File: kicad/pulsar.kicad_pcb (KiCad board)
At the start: 2 copper layers, 57 parts, among them J2 NRF-SWD, J3 XO2-JTAG, J4 CONN-2x5, Q1 NMOS, Q10 NMOS, Q11 NMOS, Q12 NMOS, Q2 NMOS, Q3 NMOS, Q4 NMOS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

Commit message: more layouting
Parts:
- added AE1: ANT, libs:ANT3216, F.Cu at (108.0, 95.5)
- added B1: nRF-BALUN, libs:BALUN-2450BM14E0003, F.Cu at (100.1, 96.1)
- added C26: 1u, SMD-1005:SMD-1005, F.Cu at (85.0, 97.0)
- added J1: POWER, libs:TERM-2-3.5-PTH, F.Cu at (125.0, 60.0)
- added J5: CONN-4, libs:CONN-4-2.54-0.8-PTH, F.Cu at (165.0, 120.0)
- added J6: CONN-4, libs:CONN-4-2.54-0.8-PTH, F.Cu at (190.0, 97.5)
- added J7: CONN-4, libs:CONN-4-2.54-0.8-PTH, F.Cu at (190.0, 82.5)
- added J8: CONN-4, libs:CONN-4-2.54-0.8-PTH, F.Cu at (170.0, 67.5)
- added S1: TACTILE-4, libs:TACT-4632, F.Cu at (80.0, 112.5)
- added S2: TACTILE-4, libs:TACT-4632, F.Cu at (72.5, 112.5)
- added Y1: 32kHz, libs:OSC2012, F.Cu at (93.0, 89.2)
- C1: value 1u -> 10u
- C12, C13, C14, C2, C3, C4, C7, C8: value C -> 100n
- C15, C5: value C -> 1u
- C16, C17: value 12pF -> 7p
- C18, C21, C24: value 100nF -> 100n
- C19, C20: value 12pF -> 6p
- C22: value 47nF -> 47n
- C23: value 2.2nF -> 2.2n
- C25: value 1nF -> 1n
- C6: value 2.2u -> 4.7u
- J2, J3: moved to B.Cu
- Y2: value 16MHz -> 32MHz; footprint osc2520:OSC2520 -> libs:OSC2016
- moved R1 63.5 mm to (130.0, 69.8)
- moved R2 63.5 mm to (131.5, 69.8)
- moved R3 63.5 mm to (125.8, 67.5)
- moved U1 63.5 mm to (125.8, 71.5)
- moved C5 47.8 mm to (162.2, 85.0), turned to 180 degrees
- moved C1 47.8 mm to (104.5, 66.2)
- moved C6 47.8 mm to (111.8, 66.5)
- moved FB1 47.8 mm to (103.0, 66.2)
- moved U3 47.8 mm to (108.0, 66.5)
- moved RT1 38.6 mm to (144.5, 108.0)
- moved C15 36.2 mm to (162.8, 95.0)
- moved Q1 29.4 mm to (161.5, 115.2), turned to 180 degrees
- moved Q2 27.8 mm to (165.0, 115.2), turned to 180 degrees
- moved Q3 27.1 mm to (168.5, 115.2), turned to 180 degrees
- moved Q4 26.9 mm to (185.2, 101.0), turned to 270 degrees
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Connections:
- C16 pad 1: PGND -> Net-(C16-Pad1)
- C16 pad 2: Net-(C16-Pad2) -> PGND
- C17 pad 1: PGND -> Net-(C17-Pad1)
- C17 pad 2: Net-(C17-Pad2) -> PGND
- C19 pad 1: PGND -> Net-(C19-Pad1)
- C19 pad 2: Net-(C19-Pad2) -> PGND
- C20 pad 1: PGND -> Net-(C20-Pad1)
- C20 pad 2: Net-(C20-Pad2) -> PGND
- U4 pad 11: Net-(U4-Pad11) -> /BUTTON1
- U4 pad 14: Net-(U4-Pad14) -> /BUTTON2
- U4 pad 15: Net-(U4-Pad15) -> /LED1
- U4 pad 16: /BUTTON1 -> /LED2
- U4 pad 17: /BUTTON2 -> /LED3
- U4 pad 19: /LED1 -> Net-(U4-Pad19)
- U4 pad 20: /LED2 -> /~XO2_RESET
- U4 pad 21: /LED3 -> /~XO2_JTAG_EN
- U4 pad 37: Net-(C19-Pad2) -> Net-(C19-Pad1)
- U4 pad 38: Net-(C20-Pad2) -> Net-(C20-Pad1)
- U4 pad 45: Net-(C16-Pad2) -> Net-(C16-Pad1)
- U4 pad 46: Net-(C17-Pad2) -> Net-(C17-Pad1)
- Y2 pad 1: Net-(C19-Pad2) -> Net-(C19-Pad1)
- Y2 pad 2: PGND -> Net-(Y2-Pad2)
- Y2 pad 3: Net-(C20-Pad2) -> Net-(C20-Pad1)
- Y2 pad 4: PGND -> Net-(Y2-Pad4)

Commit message: more layout
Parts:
- added TERM-2: VAL**, libs:TERM-2-3.5-PTH, F.Cu at (180.8, 85.5)
- added TERM-2: VAL**, libs:TERM-2-3.5-PTH, F.Cu at (180.8, 76.5)
- added TERM-2: VAL**, libs:TERM-2-3.5-PTH, F.Cu at (180.8, 94.5)
- added TERM-2: VAL**, libs:TERM-2-3.5-PTH, F.Cu at (180.8, 103.5)
- moved S2 58.1 mm to (123.0, 83.8), turned to 180 degrees
- moved S1 39.5 mm to (94.5, 75.8), turned to 270 degrees
- moved J4 38.0 mm to (106.0, 115.2), turned to 180 degrees
- moved J3 31.6 mm to (149.0, 46.5)
- moved D1 25.7 mm to (106.0, 88.2), turned to 180 degrees
- moved C26 25.6 mm to (110.5, 99.2), turned to 90 degrees
- moved D2 23.9 mm to (104.5, 88.2), turned to 180 degrees
- moved C20 22.4 mm to (94.5, 108.8), turned to 270 degrees
- moved D3 22.4 mm to (103.0, 88.2), turned to 180 degrees
- moved C17 22.3 mm to (104.5, 107.0), turned to 0 degrees
- moved R5 22.1 mm to (106.0, 90.8), turned to 180 degrees
- moved J7 21.6 mm to (170.0, 74.2), turned to 180 degrees
- moved AE1 21.2 mm to (87.5, 100.8), turned to 180 degrees
- moved RT1 20.6 mm to (155.0, 90.2)
- moved Y1 20.1 mm to (102.5, 107.0), turned to 0 degrees
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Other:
- board outline added: 50 x 50 mm

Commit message: antenna feed calculations
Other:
- board text added: "50R Antenna feed on FR-4 1.2mm/1.6mm: coplanar wave guide with ground plane, 750um conductor, 160um spacing (see antenna_waveguide.xsctn)"
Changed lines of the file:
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@@
     (area 0 0 0 0)
     (thickness 1.6)
-    (drawings 7)
+    (drawings 8)
     (tracks 0)
     (zones 0)
@@
     (pad 2 thru_hole oval (at 1.75 0 90) (size 2 2.6) (drill 1.2) (layers *.Cu *.Mask))
   )
+  (gr_text "50R Antenna feed on FR-4 1.2mm/1.6mm:\ncoplanar wave guide with ground plane,\n750um conductor, 160um spacing\n(see antenna_waveguide.xsctn)" (at 25.75 81.25) (layer Cmts.User)
+    (effects (font (size 1.5 1.5) (thickness 0.05)) (justify left))
+  )
   (gr_circle (center 212.25 124.75) (end 214.75 124.75) (layer Dwgs.User) (width 0.2))

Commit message: layout progress
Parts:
- removed TERM-2 (x4): VAL**, libs:TERM-2-3.5-PTH
- added J13: CONN-2, libs:TERM-2-3.5-PTH, F.Cu at (146.0, 139.2)
- added J14: CONN-2, libs:TERM-2-3.5-PTH, F.Cu at (146.0, 129.8)
- added J15: CONN-2, libs:TERM-2-3.5-PTH, F.Cu at (146.0, 120.2)
- added J16: CONN-2, libs:TERM-2-3.5-PTH, F.Cu at (146.0, 110.8)
- added MH1: MOUNTHOLE, libs:HOLE-M3-COND, F.Cu at (135.0, 135.0)
- added MH2: MOUNTHOLE, libs:HOLE-M3-COND, F.Cu at (115.0, 135.0)
- added MH3: MOUNTHOLE, libs:HOLE-M3-COND, F.Cu at (115.0, 115.0)
- added MH4: MOUNTHOLE, libs:HOLE-M3-COND, F.Cu at (135.0, 115.0)
- C1: footprint SMD-1005:SMD-1005 -> SMD-2012:SMD-2012
- R1, R2: footprint SMD-1608:SMD-1608 -> SMD-1005:SMD-1005
- moved J3 72.0 mm to (122.0, 113.2), turned to 90 degrees
- moved Q1 56.0 mm to (128.0, 143.0)
- moved Q7 53.3 mm to (139.5, 120.0), turned to 270 degrees
- moved Q2 50.5 mm to (131.5, 143.0)
- moved Q3 50.5 mm to (135.0, 143.0)
- moved Q4 50.4 mm to (138.5, 143.0), turned to 180 degrees
- moved C12 50.2 mm to (133.0, 130.0)
- moved C13 50.2 mm to (126.8, 125.5)
- moved C14 50.2 mm to (126.8, 126.5)
- moved C15 50.2 mm to (132.0, 130.0)
- moved C2 50.2 mm to (136.8, 123.2)
- moved C3 50.2 mm to (136.8, 125.8)
- moved C4 50.2 mm to (130.5, 120.0)
- moved C7 50.2 mm to (126.8, 123.8)
- moved C8 50.2 mm to (136.8, 126.8)
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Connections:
- net Net-(J5-Pad2) renamed /rgb1/CH1_OUT
- net Net-(J5-Pad3) renamed /rgb1/CH2_OUT
- net Net-(J5-Pad4) renamed /rgb1/CH3_OUT
- net Net-(J6-Pad2) renamed /rgb2/CH1_OUT
- net Net-(J6-Pad3) renamed /rgb2/CH2_OUT
- net Net-(J6-Pad4) renamed /rgb2/CH3_OUT
- net Net-(J7-Pad2) renamed /rgb3/CH1_OUT
- net Net-(J7-Pad3) renamed /rgb3/CH2_OUT
- net Net-(J7-Pad4) renamed /rgb3/CH3_OUT
- net Net-(J8-Pad2) renamed /rgb4/CH1_OUT
- net Net-(J8-Pad3) renamed /rgb4/CH2_OUT
- net Net-(J8-Pad4) renamed /rgb4/CH3_OUT
- C10 pad 1: /IIN_SENSE -> /VIN_SENSE
- C11 pad 1: /TEMP_SENSE -> /IIN_SENSE
- C9 pad 1: /VIN_SENSE -> /TEMP_SENSE
- J2 pad 10: Net-(J2-Pad10) -> (no net)
- J2 pad 7: Net-(J2-Pad7) -> (no net)
- J2 pad 9: Net-(J2-Pad9) -> (no net)
- J3 pad 7: Net-(J3-Pad7) -> (no net)
- J4 pad 1: /AUX1 -> +3V3
- J4 pad 3: /AUX2 -> /AUX1
- J4 pad 5: /AUX3 -> /AUX2
- J4 pad 7: /AUX4 -> /AUX3
- J4 pad 9: /AUX5 -> /AUX4
- S1 pad 2: Net-(S1-Pad2) -> (no net)
- S2 pad 2: Net-(S2-Pad2) -> (no net)
- U3 pad 4: Net-(U3-Pad4) -> (no net)
- U4 pad 10: Net-(U4-Pad10) -> (no net)
- U4 pad 11: /BUTTON1 -> (no net)
- U4 pad 14: /BUTTON2 -> (no net)
- U4 pad 18: Net-(U4-Pad18) -> /BUTTON1
- U4 pad 19: Net-(U4-Pad19) -> /BUTTON2
- U4 pad 2: Net-(U4-Pad2) -> (no net)
- U4 pad 3: /AUX5 -> /AUX1
- U4 pad 31: Net-(B1-Pad3) -> Net-(B1-Pad4)
- U4 pad 32: Net-(B1-Pad4) -> Net-(B1-Pad3)
- U4 pad 4: /AUX1 -> /AUX2
- U4 pad 5: /AUX2 -> (no net)
- U4 pad 6: /VIN_SENSE -> /TEMP_SENSE
- U4 pad 7: /IIN_SENSE -> /VIN_SENSE
- U4 pad 8: /TEMP_SENSE -> /IIN_SENSE
- U4 pad 9: Net-(U4-Pad9) -> (no net)
- Y2 pad 2: Net-(Y2-Pad2) -> (no net)
- Y2 pad 4: Net-(Y2-Pad4) -> (no net)
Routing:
- net +3V3: track 0.00 -> 24.8 mm
- net /ANT: track 0.00 -> 15.3 mm
- net /VIN_SENSE: track 0.00 -> 14.5 mm
- net /IIN_SENSE: track 0.00 -> 13.1 mm
- net Net-(C17-Pad1): track 0.00 -> 6.34 mm
- net Net-(C20-Pad1): track 0.00 -> 5.91 mm
- net Net-(C16-Pad1): track 0.00 -> 5.90 mm
- net Net-(C19-Pad1): track 0.00 -> 3.51 mm
- net Net-(B1-Pad5): track 0.00 -> 3.40 mm
- net /TEMP_SENSE: track 0.00 -> 3.02 mm
- net Net-(C22-Pad1): track 0.00 -> 2.88 mm
- net Net-(C24-Pad1): track 0.00 -> 2.17 mm
- net Net-(B1-Pad4): track 0.00 -> 1.51 mm
- net Net-(B1-Pad3): track 0.00 -> 1.51 mm
- added copper zone on B.Cu, net DGND
- added copper zone on F.Cu, net DGND
- added copper zone on B.Cu, net VIN
- added copper zone on F.Cu, net VIN
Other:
- net class Default: clearance 0.15 -> 0.1499; trace_width 0.15 -> 0.1499; via_dia 0.6 -> 0.55
- net class antenna feed added: clearance 0.16, trace_width 0.75, via_dia 0.55, via_drill 0.3
- rule trace_clearance: 0.15 -> 0.1499
- rule trace_min: 0.15 -> 0.1499
- rule via_min_size: 0.6 -> 0.55

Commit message: more layout
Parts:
- moved C14 10.9 mm to (137.2, 123.8), turned to 90 degrees
- moved C12 10.3 mm to (130.5, 120.0), turned to 180 degrees
- moved C5 10.0 mm to (135.0, 130.0), turned to 0 degrees
- moved C7 7.72 mm to (133.5, 120.0), turned to 180 degrees
- moved C2 7.29 mm to (134.0, 130.0), turned to 0 degrees
- moved C4 7.29 mm to (137.2, 122.8), turned to 90 degrees
- moved C13 7.27 mm to (131.5, 120.0), turned to 180 degrees
- moved C8 7.27 mm to (130.2, 130.0), turned to 0 degrees
- moved C3 6.95 mm to (131.2, 130.0), turned to 0 degrees
- moved C15 6.05 mm to (127.2, 126.2), turned to 270 degrees
- moved C16 4.17 mm to (117.3, 122.4), turned to 180 degrees
- moved C17 2.24 mm to (113.3, 122.4), turned to 180 degrees
- moved Y1 1.79 mm to (115.3, 122.4), turned to 180 degrees
- moved C19 0.79 mm to (113.2, 129.0)
- moved C20 0.79 mm to (116.8, 129.0)
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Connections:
- B1 pad 2: PGND -> DGND
- B1 pad 6: PGND -> DGND
- C1 pad 2: PGND -> DGND
- C10 pad 2: PGND -> DGND
- C11 pad 2: PGND -> DGND
- C12 pad 2: PGND -> DGND
- C13 pad 2: PGND -> DGND
- C14 pad 2: PGND -> DGND
- C15 pad 2: PGND -> DGND
- C16 pad 2: PGND -> DGND
- C17 pad 2: PGND -> DGND
- C18 pad 2: PGND -> DGND
- C19 pad 2: PGND -> DGND
- C2 pad 2: PGND -> DGND
- C20 pad 2: PGND -> DGND
- C21 pad 2: PGND -> DGND
- C22 pad 2: PGND -> DGND
- C23 pad 2: PGND -> DGND
- C24 pad 2: PGND -> DGND
- C25 pad 2: PGND -> DGND
- C26 pad 2: PGND -> DGND
- C3 pad 2: PGND -> DGND
- C4 pad 2: PGND -> DGND
- C5 pad 2: PGND -> DGND
- C6 pad 2: PGND -> DGND
- C7 pad 2: PGND -> DGND
- C8 pad 2: PGND -> DGND
- C9 pad 2: PGND -> DGND
- D1 pad C: PGND -> DGND
- D2 pad C: PGND -> DGND
- D3 pad C: PGND -> DGND
- J1 pad 2: PGND -> DGND
- J2 pad 3: PGND -> DGND
- J2 pad 5: PGND -> DGND
- J3 pad 2: /XO2_JTAG_TMS -> /rgb2/CH3
- J3 pad 3: PGND -> DGND
- J3 pad 4: /XO2_JTAG_TCK -> /rgb3/CH1
- J3 pad 5: PGND -> DGND
- J3 pad 6: /XO2_JTAG_TDO -> /rgb3/CH3
- J3 pad 8: /XO2_JTAG_TDI -> /rgb3/CH2
- J4 pad 10: PGND -> DGND
- MH1 pad 1: PGND -> DGND
- MH2 pad 1: PGND -> DGND
- MH3 pad 1: PGND -> DGND
- MH4 pad 1: PGND -> DGND
- Q1 pad S: PGND -> DGND
- Q10 pad S: PGND -> DGND
- Q11 pad S: PGND -> DGND
- Q12 pad S: PGND -> DGND
- Q2 pad S: PGND -> DGND
- Q3 pad S: PGND -> DGND
- Q4 pad S: PGND -> DGND
- Q5 pad S: PGND -> DGND
- Q6 pad S: PGND -> DGND
- Q7 pad S: PGND -> DGND
- Q8 pad S: PGND -> DGND
- Q9 pad S: PGND -> DGND
- R2 pad 2: PGND -> DGND
- RT1 pad 2: PGND -> DGND
- S1 pad 3: PGND -> DGND
- S1 pad 4: PGND -> DGND
- S2 pad 3: PGND -> DGND
- S2 pad 4: PGND -> DGND
- U1 pad 1: PGND -> DGND
- U1 pad 2: PGND -> DGND
- U2 pad 1: /XO2_JTAG_TDO -> /rgb3/CH3
- U2 pad 11: /rgb2/CH1 -> (no net)
- U2 pad 12: /rgb2/CH2 -> (no net)
- U2 pad 13: /rgb2/CH3 -> (no net)
- U2 pad 14: /rgb3/CH1 -> /SPI_CS
- U2 pad 16: /SPI_CS -> /SPI_CS_PGM
- U2 pad 20: /rgb3/CH2 -> /rgb1/CH1
- U2 pad 21: /rgb3/CH3 -> /rgb1/CH2
- U2 pad 22: PGND -> DGND
- U2 pad 23: /rgb4/CH1 -> /rgb1/CH3
- U2 pad 27: /rgb4/CH2 -> /rgb2/CH1
- U2 pad 28: /rgb4/CH3 -> /rgb2/CH2
- U2 pad 29: /XO2_JTAG_TMS -> /rgb2/CH3
- U2 pad 3: PGND -> DGND
- U2 pad 30: /XO2_JTAG_TCK -> /rgb3/CH1
- U2 pad 32: /XO2_JTAG_TDI -> /rgb3/CH2
- U2 pad 4: /rgb1/CH1 -> /rgb4/CH1
- U2 pad 5: /rgb1/CH2 -> /rgb4/CH2
- U2 pad 8: /rgb1/CH3 -> /rgb4/CH3
- U2 pad FLAG: PGND -> DGND
- U3 pad 2: PGND -> DGND
- U4 pad 13: PGND -> DGND
- U4 pad 20: /~XO2_RESET -> (no net)
- U4 pad 21: /~XO2_JTAG_EN -> (no net)
- U4 pad 22: /XO2_JTAG_TDO -> (no net)
- U4 pad 27: /XO2_JTAG_TMS -> (no net)
- U4 pad 28: /XO2_JTAG_TCK -> (no net)
- U4 pad 33: PGND -> DGND
- U4 pad 34: PGND -> DGND
- U4 pad 40: /XO2_JTAG_TDI -> /SPI_MOSI
- U4 pad 41: /SPI_CLK -> /SPI_CS_PGM
- U4 pad 42: /SPI_MISO -> /SPI_CS
- U4 pad 43: /SPI_CS -> /SPI_MISO
- U4 pad 44: /SPI_MOSI -> /SPI_CLK
- U4 pad 47: /AUX3 -> /~XO2_RESET
- U4 pad 5: (no net) -> /AUX3
- U4 pad FLAG: PGND -> DGND
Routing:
- net +3V3: track 24.8 -> 57.8 mm
- net /rgb2/CH3_OUT: track 0.00 -> 25.8 mm
- net /rgb3/CH1_OUT: track 0.00 -> 23.2 mm
- net DGND: track 0.00 -> 22.4 mm, vias 0 -> 10
- net /rgb2/CH2_OUT: track 0.00 -> 14.3 mm
- net /rgb2/CH1: track 0.00 -> 13.3 mm, vias 0 -> 2
- net /rgb3/CH2_OUT: track 0.00 -> 12.5 mm
- net /rgb1/CH3: track 0.00 -> 12.1 mm, vias 0 -> 2
- net /rgb3/CH3: track 0.00 -> 11.3 mm, vias 0 -> 2
- net /rgb4/CH1: track 0.00 -> 11.2 mm, vias 0 -> 2
- net /rgb4/CH3: track 0.00 -> 10.7 mm, vias 0 -> 2
- net /rgb4/CH2: track 0.00 -> 10.5 mm, vias 0 -> 2
- net /rgb1/CH2: track 0.00 -> 10.1 mm, vias 0 -> 2
- net /rgb1/CH1: track 0.00 -> 9.62 mm, vias 0 -> 2
- net (no net): track 0.00 -> 8.88 mm, vias 0 -> 1
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- added copper zone on B.Cu, net PGND
- added copper zone on F.Cu, net PGND
- removed copper zone on B.Cu, net DGND
- removed copper zone on F.Cu, net DGND
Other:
- net class high current added: clearance 0.15, trace_width 0.5, via_dia 0.55, via_drill 0.3

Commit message: layout
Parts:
- moved D1 22.8 mm to (102.2, 119.2), turned to 270 degrees
- moved D2 22.3 mm to (102.2, 121.8), turned to 270 degrees
- moved D3 22.1 mm to (102.2, 124.2), turned to 270 degrees
- moved C6 21.5 mm to (101.5, 103.0), turned to 180 degrees
- moved J3 20.2 mm to (138.4, 125.0), turned to 180 degrees
- moved R5 20.1 mm to (104.5, 119.5)
- moved R6 19.4 mm to (104.5, 122.0)
- moved R7 19.0 mm to (104.5, 124.5)
- moved U3 15.6 mm to (104.5, 103.0), turned to 90 degrees
- moved J1 10.8 mm to (115.2, 104.2)
- moved R3 10.5 mm to (122.0, 102.2)
- moved U1 10.5 mm to (122.0, 105.5)
- moved C1 9.42 mm to (107.8, 103.0), turned to 180 degrees
- moved C26 8.00 mm to (113.8, 120.0)
- moved FB1 7.22 mm to (109.5, 102.5), turned to 0 degrees
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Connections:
- C10 pad 1: /VIN_SENSE -> /IIN_SENSE
- C11 pad 1: /IIN_SENSE -> /VIN_SENSE
- J3 pad 2: /rgb2/CH3 -> /XO2_JTAG_TMS
- J3 pad 4: /rgb3/CH1 -> /XO2_JTAG_TCK
- J3 pad 6: /rgb3/CH3 -> /rgb3/CH1
- J3 pad 8: /rgb3/CH2 -> /rgb2/CH3
- S1 pad 1: /BUTTON1 -> (no net)
- S1 pad 2: (no net) -> /BUTTON1
- S2 pad 1: /BUTTON2 -> (no net)
- S2 pad 2: (no net) -> /BUTTON2
- U2 pad 1: /rgb3/CH3 -> /rgb3/CH1
- U2 pad 11: (no net) -> /SPI_CS
- U2 pad 12: (no net) -> /rgb4/CH2
- U2 pad 13: (no net) -> /rgb4/CH3
- U2 pad 14: /SPI_CS -> (no net)
- U2 pad 29: /rgb2/CH3 -> /XO2_JTAG_TMS
- U2 pad 30: /rgb3/CH1 -> /XO2_JTAG_TCK
- U2 pad 32: /rgb3/CH2 -> /rgb2/CH3
- U2 pad 4: /rgb4/CH1 -> /rgb3/CH2
- U2 pad 5: /rgb4/CH2 -> /rgb3/CH3
- U2 pad 8: /rgb4/CH3 -> /rgb4/CH1
- U4 pad 7: /VIN_SENSE -> /IIN_SENSE
- U4 pad 8: /IIN_SENSE -> /VIN_SENSE
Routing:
- net /SPI_CLK: track 3.27 -> 33.3 mm
- net /SPI_MISO: track 3.62 -> 33.0 mm
- net /SPI_CS: track 3.19 -> 31.7 mm
- net /SPI_MOSI: track 2.91 -> 30.4 mm, vias 2 -> 0
- net /IIN_SENSE: track 13.1 -> 40.5 mm, vias 0 -> 2
- net /rgb3/CH1: track 1.00 -> 28.3 mm, vias 1 -> 2
- net VIN: track 0.00 -> 26.5 mm
- net DGND: track 22.4 -> 46.0 mm, vias 10 -> 29
- net /TEMP_SENSE: track 3.02 -> 25.0 mm, vias 0 -> 2
- net /BUTTON1: track 0.00 -> 20.7 mm
- net /RX: track 0.00 -> 20.5 mm, vias 0 -> 1
- net /TX: track 0.30 -> 20.6 mm, vias 0 -> 1
- net /NRF_SWDIO/~RESET: track 0.00 -> 19.8 mm, vias 0 -> 1
- net /rgb2/CH3: track 1.50 -> 21.2 mm, vias 1 -> 2
- net /NRF_SWDCLK: track 0.00 -> 19.7 mm, vias 0 -> 1
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- added copper zone on B.Cu, net DGND
- added copper zone on F.Cu, net DGND
- removed copper zone on B.Cu, net PGND
- removed copper zone on F.Cu, net PGND

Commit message: layout
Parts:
- moved C15 0.25 mm to (123.0, 126.2), turned to 180 degrees
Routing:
- net +3V3: track 51.4 -> 142.8 mm, vias 1 -> 8
- net /~XO2_RESET: track 14.4 -> 57.0 mm, vias 1 -> 3
- net DGND: track 46.0 -> 48.7 mm, vias 29 -> 32
- net /TEMP_SENSE: track 25.0 -> 26.6 mm
- net /rgb1/CH3: track 17.3 -> 18.2 mm
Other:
- net class power supply added: clearance 0.1499, trace_width 0.3, via_dia 0.55, via_drill 0.3

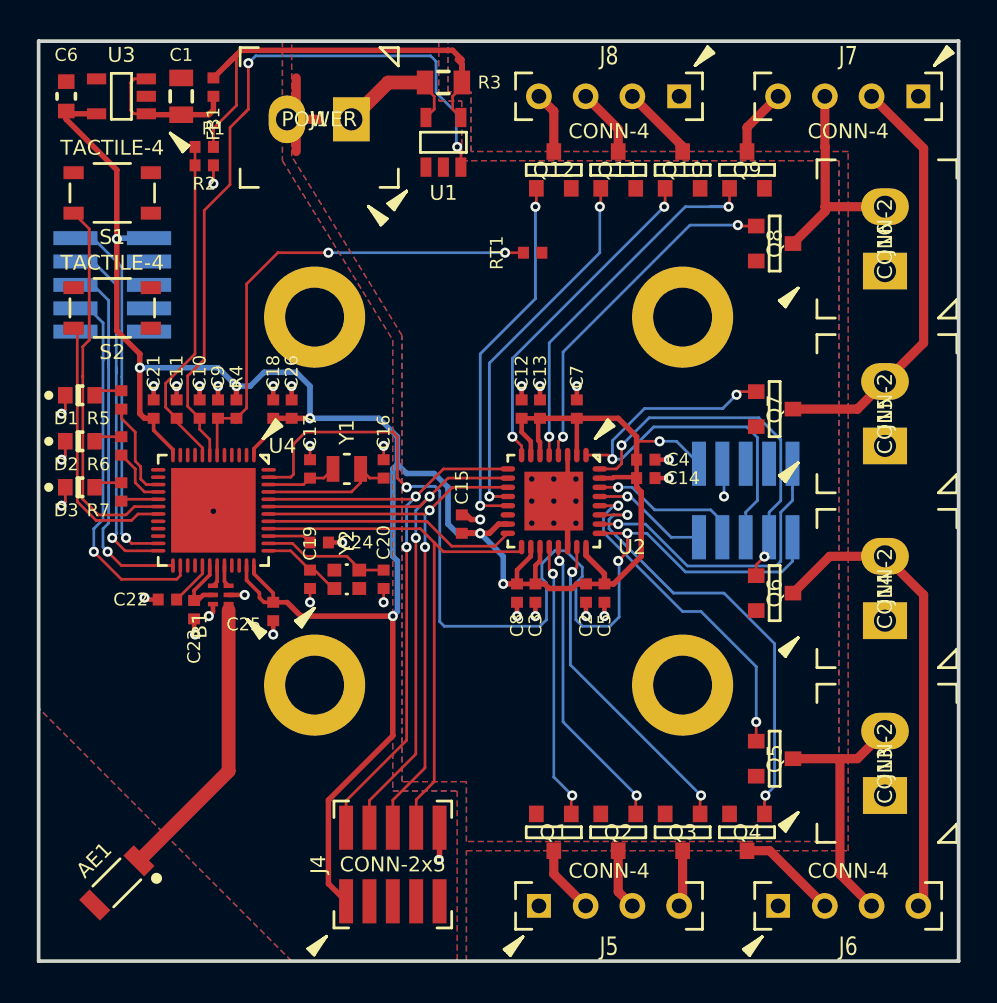
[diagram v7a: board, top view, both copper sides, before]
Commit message: switch to 4 layers
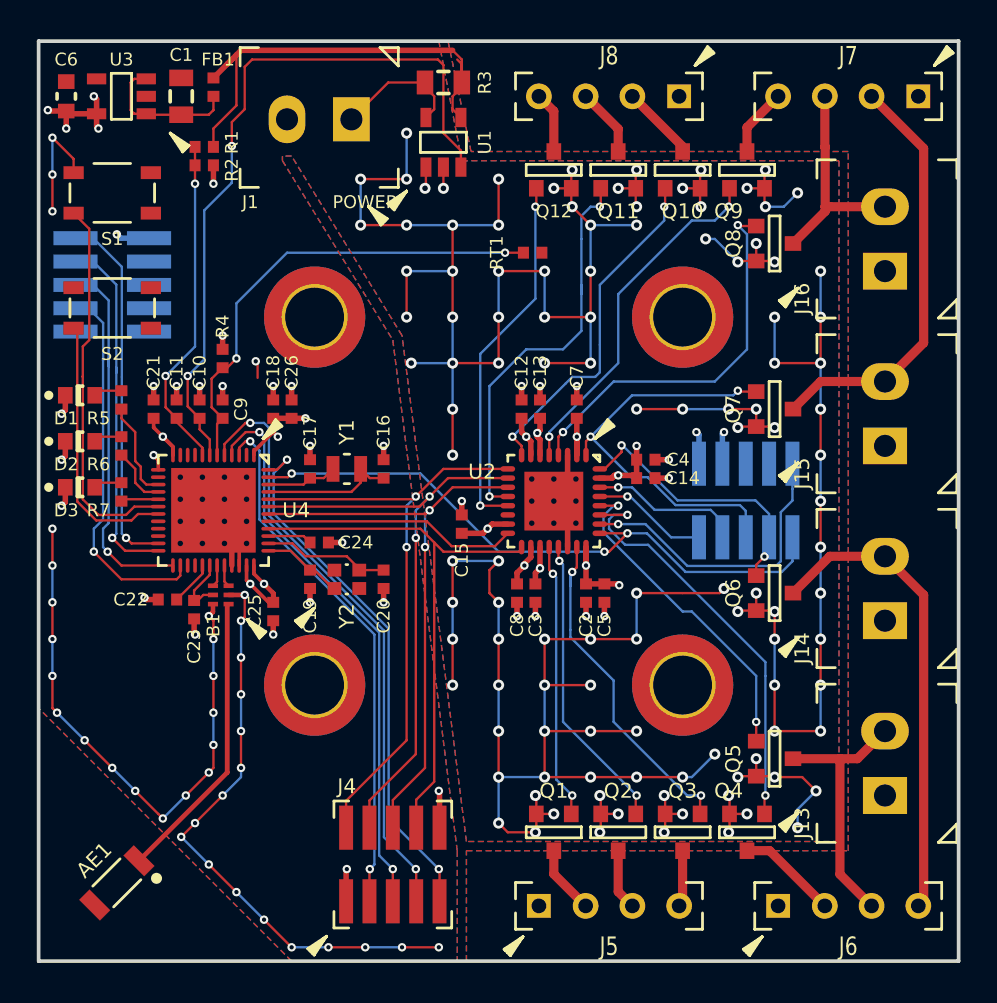
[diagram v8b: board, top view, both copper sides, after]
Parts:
- moved R4 2.85 mm to (110.0, 117.2)
- moved C9 0.25 mm to (110.0, 120.0)
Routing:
- net DGND: track 48.7 -> 343.5 mm, vias 32 -> 182
- net +3V3: track 142.8 -> 49.9 mm, vias 8 -> 23
- net /AUX3: track 0.00 -> 32.7 mm, vias 0 -> 2
- net /AUX2: track 0.00 -> 30.8 mm, vias 0 -> 2
- net /AUX4: track 0.00 -> 29.6 mm, vias 0 -> 2
- net /AUX1: track 0.00 -> 29.1 mm, vias 0 -> 2
- net /~XO2_RESET: track 57.0 -> 35.0 mm
- net /rgb2/CH3: track 21.2 -> 16.3 mm
- net /rgb3/CH1: track 28.3 -> 25.0 mm
- net /rgb3/CH2: track 19.1 -> 21.2 mm
- net /rgb4/CH2: track 20.3 -> 22.2 mm
- net /rgb3/CH3: track 20.9 -> 19.3 mm
- net /rgb2/CH1: track 24.2 -> 22.9 mm
- net (no net): track 0.00 -> 0.94 mm, vias 0 -> 1
- net /rgb4/CH1: track 18.4 -> 19.1 mm
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- added copper zone on In2.Cu, net +3V3
- added copper zone on In1.Cu, net DGND
- added copper zone on In1.Cu, net VIN
- added copper zone on In2.Cu, net VIN
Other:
- copper layers 2 -> 4
- net class Default: clearance 0.1499 -> 0.129; trace_width 0.1499 -> 0.129; via_dia 0.55 -> 0.46; via_drill 0.3 -> 0.25
- net class antenna feed: clearance 0.16 -> 0.135; trace_width 0.75 -> 0.26
- net class high current: clearance 0.15 -> 0.129; via_dia 0.55 -> 0.46; via_drill 0.3 -> 0.25
- net class power supply: clearance 0.1499 -> 0.129; via_dia 0.55 -> 0.46; via_drill 0.3 -> 0.25
- rule trace_clearance: 0.1499 -> 0.129
- rule trace_min: 0.1499 -> 0.129
- rule via_min_drill: 0.3 -> 0.25
- rule via_min_size: 0.55 -> 0.46
- board text added: "50R Antenna feed on FR-408 170um coplanar wave guide with ground plane, 260um conductor, 135um spacing (see antenna_waveguide_4l.xsctn)"
- board text removed: "50R Antenna feed on FR-4 1.2mm/1.6mm: coplanar wave guide with ground plane, 750um conductor, 160um spacing (see antenna_waveguide.xsctn)"
